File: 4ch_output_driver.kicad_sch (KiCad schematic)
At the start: 9 parts, among them U7 LTV-247

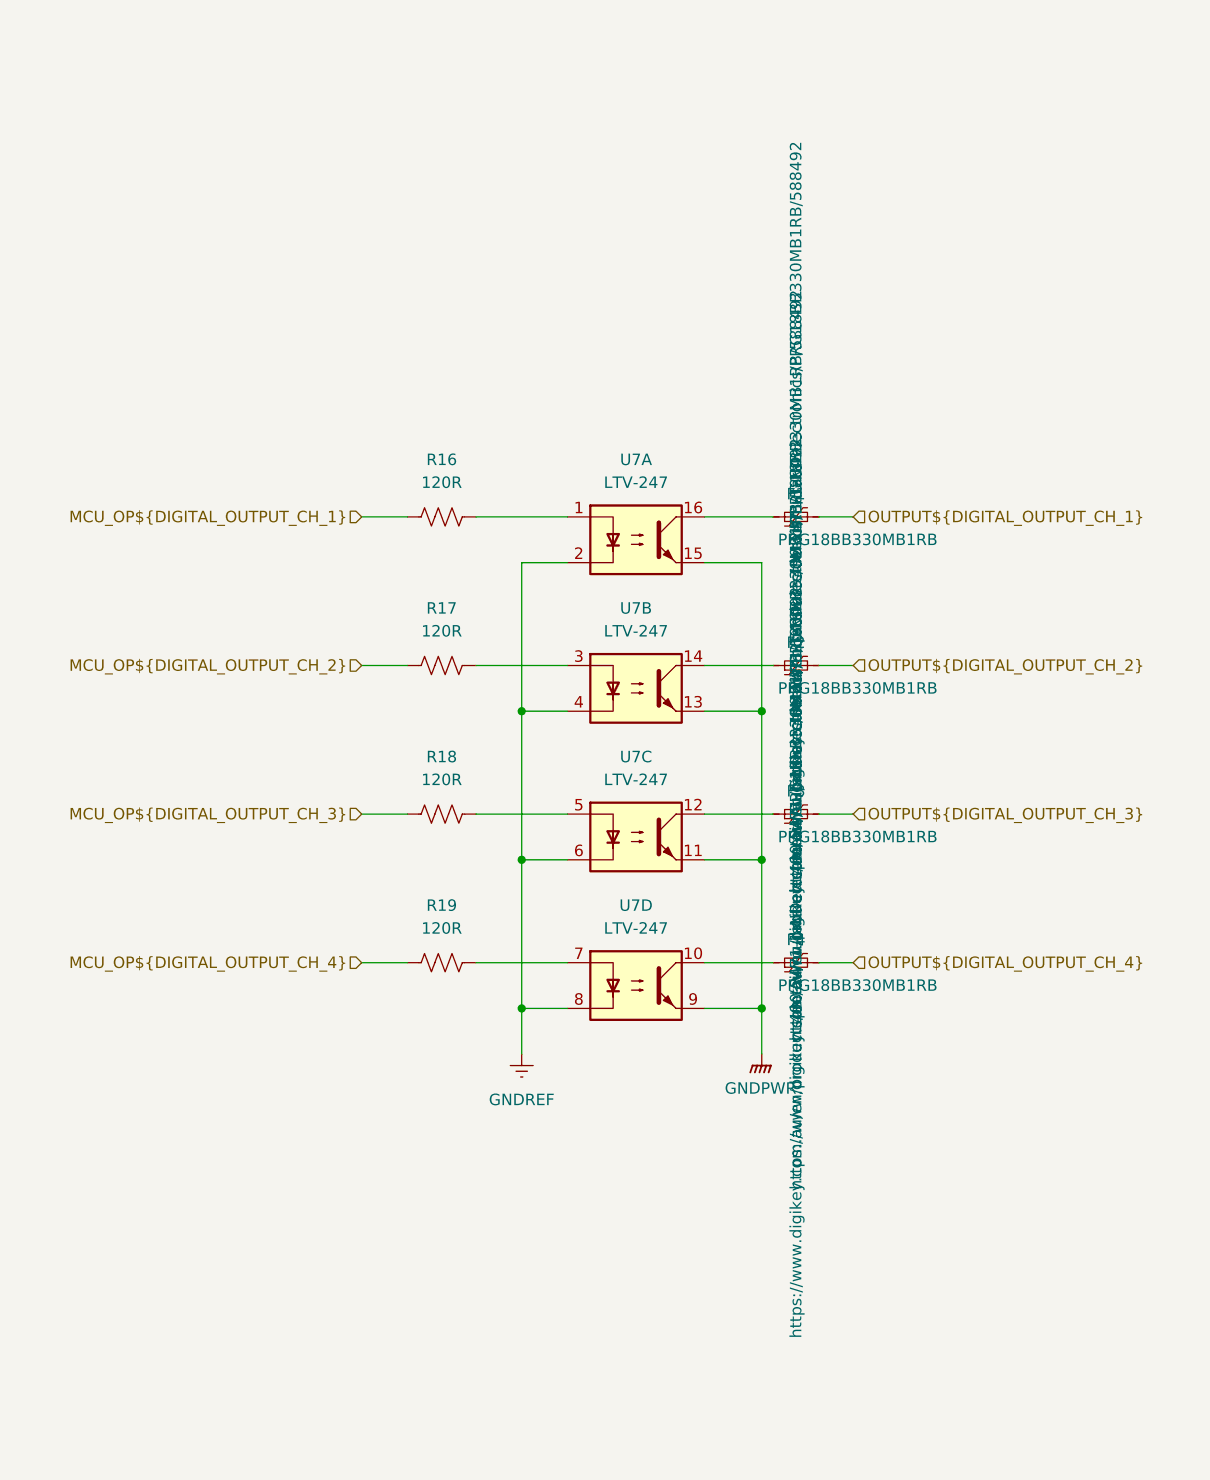
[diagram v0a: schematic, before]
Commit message: fix to annoying additional symbol fields displaying when we didn't want them to.
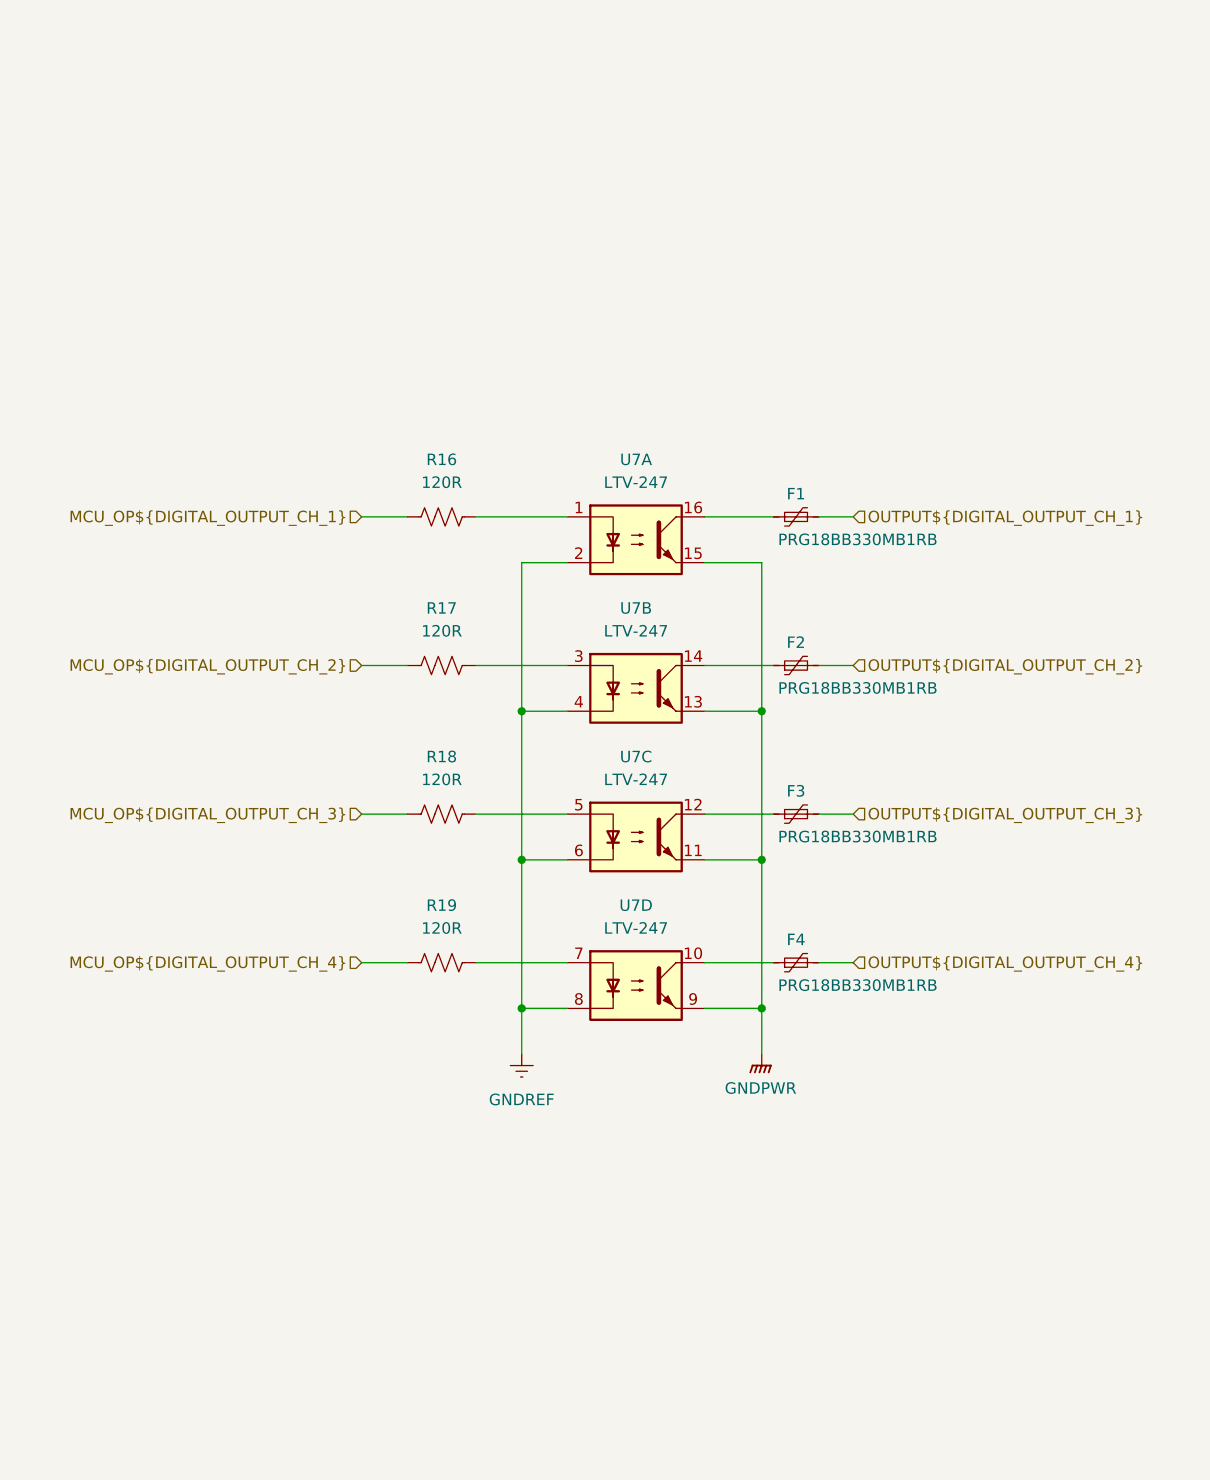
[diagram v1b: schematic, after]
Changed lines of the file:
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@@
 					(size 1.27 1.27)
 				)
+				(hide yes)
 			)
 		)
@@
 					(size 1.27 1.27)
 				)
+				(hide yes)
 			)
 		)
@@
 					(size 1.27 1.27)
 				)
+				(hide yes)
 			)
 		)
@@
 					(size 1.27 1.27)
 				)
+				(hide yes)
 			)
 		)
@@
 					(size 1.27 1.27)
 				)
+				(hide yes)
 			)
 		)
@@
 					(size 1.27 1.27)
 				)
+				(hide yes)
 			)
 		)
@@
 					(size 1.27 1.27)
 				)
+				(hide yes)
 			)
 		)
@@
 					(size 1.27 1.27)
 				)
+				(hide yes)
 			)
 		)
@@
 					(size 1.27 1.27)
 				)
+				(hide yes)
 			)
 		)
@@
 					(size 1.27 1.27)
 				)
+				(hide yes)
 			)
 		)
@@
 					(size 1.27 1.27)
 				)
+				(hide yes)
 			)
 		)
@@
 					(size 1.27 1.27)
 				)
+				(hide yes)
 			)
 		)
@@
 					(size 1.27 1.27)
 				)
+				(hide yes)
 			)
 		)
@@
 					(size 1.27 1.27)
 				)
+				(hide yes)
 			)
 		)
@@
 					(size 1.27 1.27)
 				)
+				(hide yes)
 			)
 		)
@@
 					(size 1.27 1.27)
 				)
+				(hide yes)
 			)
 		)
@@
 					(size 1.27 1.27)
 				)
+				(hide yes)
 			)
 		)
@@
 					(size 1.27 1.27)
 				)
+				(hide yes)
 			)
 		)
@@
 					(size 1.27 1.27)
 				)
+				(hide yes)
 			)
 		)
@@
 					(size 1.27 1.27)
 				)
+				(hide yes)
 			)
 		)
@@
 					(size 1.27 1.27)
 				)
+				(hide yes)
 			)
 		)
@@
 					(size 1.27 1.27)
 				)
+				(hide yes)
 			)
 		)
@@
 					(size 1.27 1.27)
 				)
+				(hide yes)
 			)
 		)
@@
 					(size 1.27 1.27)
 				)
-			)
-		)
+				(hide yes)
+			)
+		)

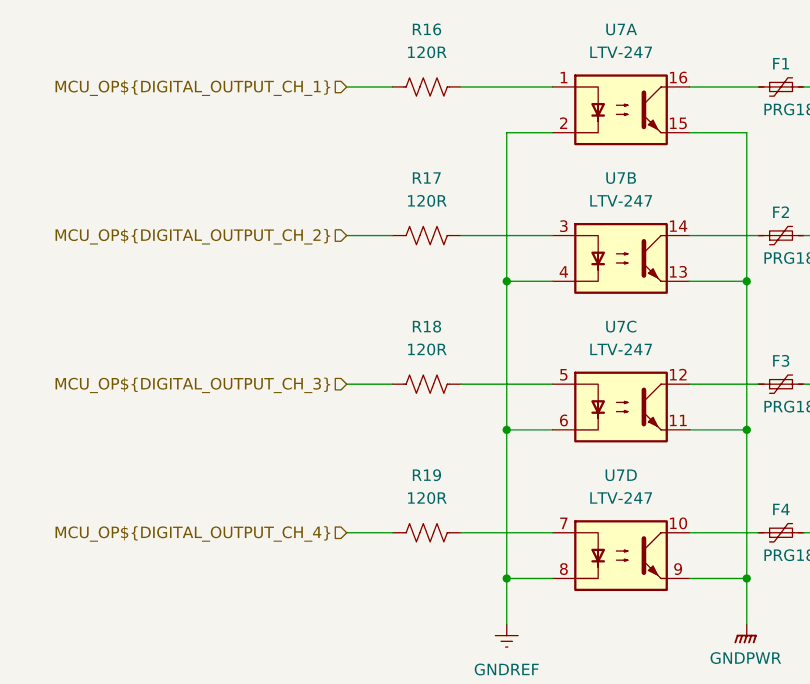
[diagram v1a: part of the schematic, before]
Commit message: BOM consolidation for various resistors. Moved BOM into symbol libraries and updated supplimentary BOM. Switched IO optical isolation circuitry to a more cost effective part.
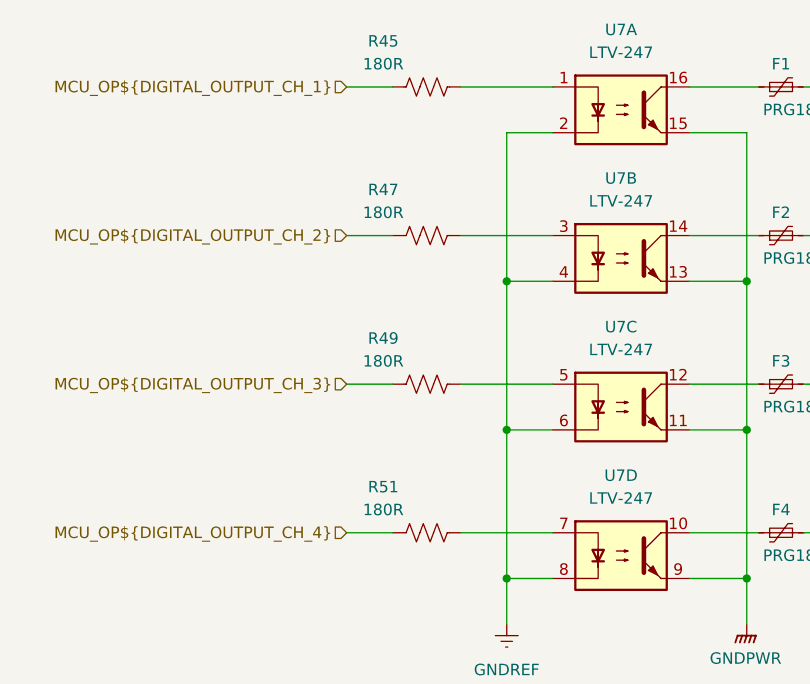
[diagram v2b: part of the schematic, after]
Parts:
- removed R16, R17, R18, R19: 120R, Resistor_SMD:R_1206_3216Metric_Pad1.30x1.75mm_HandSolder, symbol Device:R_US
- added R45, R47, R49, R51: 180R, Resistor_SMD:R_1206_3216Metric_Pad1.30x1.75mm_HandSolder, symbol Device:R_US
- U7: Digikey Part Number (none) -> 160-2255-1-ND; Digikey URL (none) -> https://www.digikey.com.au/en/products/detail/lite-on-inc/l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
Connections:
- net MCU_OP${DIGITAL_OUTPUT_CH_1}: now also R45.1
- net MCU_OP${DIGITAL_OUTPUT_CH_2}: now also R47.1
- net MCU_OP${DIGITAL_OUTPUT_CH_3}: now also R49.1
- net MCU_OP${DIGITAL_OUTPUT_CH_4}: now also R51.1
- net at U7.5: now also R49.2
- net at U7.7: now also R51.2
- net at U7.1: now also R45.2
- net at U7.3: now also R47.2

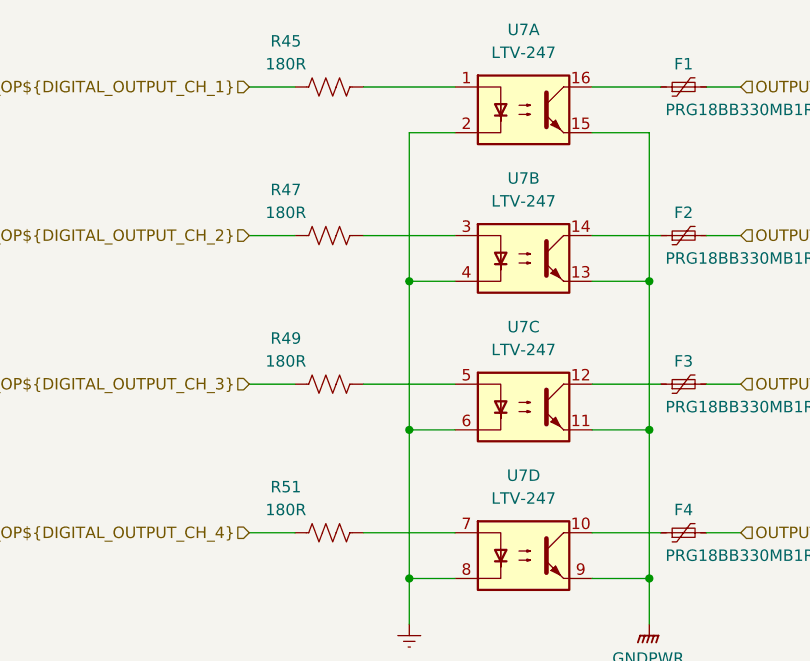
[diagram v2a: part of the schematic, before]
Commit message: New PSU designs + footprints assigned. Changes to board shape to make room for new components. BOM consolidation of supplimentary file
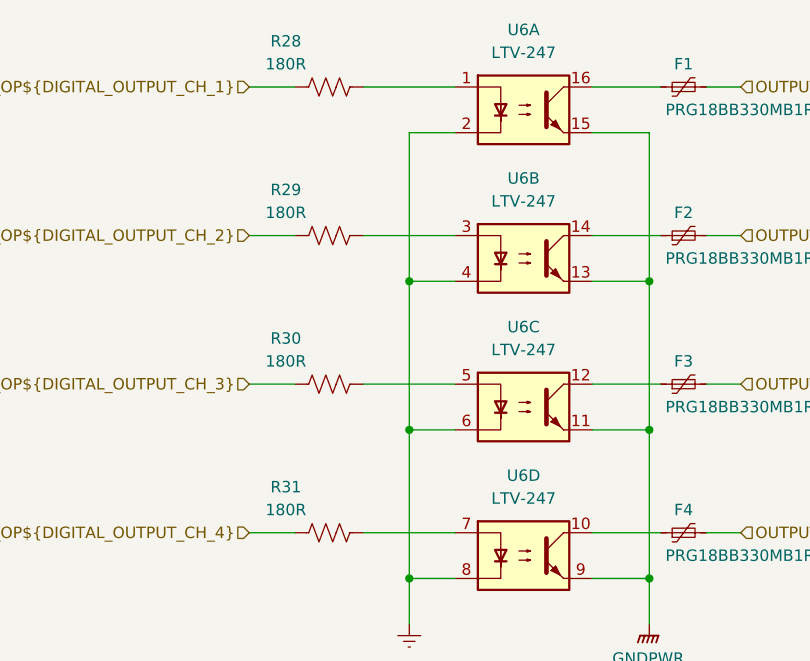
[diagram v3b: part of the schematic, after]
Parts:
- renumbered R45 to R28, R47 to R29, R49 to R30, R51 to R31, U7 to U6
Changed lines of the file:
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@@
 		(dnp no)
 		(fields_autoplaced yes)
-		(property "Reference" "U7"
+		(property "Reference" "U6"
 			(at 144.78 95.25 0)
 			(effects
@@
 				)
 				(path "/5473abc6-7b93-43cc-a401-f691c4d7d7cf/a10f9653-3098-46b3-8571-958500eea49a/75bfee9f-dba1-4332-b42b-f74c9030c21f"
-					(reference "U7")
+					(reference "U6")
 					(unit 3)
 				)
@@
 		(dnp no)
 		(fields_autoplaced yes)
-		(property "Reference" "U7"
+		(property "Reference" "U6"
 			(at 144.78 111.76 0)
 			(effects
@@
 				)
 				(path "/5473abc6-7b93-43cc-a401-f691c4d7d7cf/a10f9653-3098-46b3-8571-958500eea49a/75bfee9f-dba1-4332-b42b-f74c9030c21f"
-					(reference "U7")
+					(reference "U6")
 					(unit 4)
 				)
@@
 		(dnp no)
 		(fields_autoplaced yes)
-		(property "Reference" "U7"
+		(property "Reference" "U6"
 			(at 144.78 62.23 0)
 			(effects
@@
 				)
 				(path "/5473abc6-7b93-43cc-a401-f691c4d7d7cf/a10f9653-3098-46b3-8571-958500eea49a/75bfee9f-dba1-4332-b42b-f74c9030c21f"
-					(reference "U7")
+					(reference "U6")
 					(unit 1)
 				)
@@
 		(on_board yes)
 		(dnp no)
-		(property "Reference" "R49"
+		(property "Reference" "R30"
 			(at 118.364 96.52 90)
 			(effects
@@
 			(project "Remora Nucleo F446ZE Hat"
 				(path "/5473abc6-7b93-43cc-a401-f691c4d7d7cf/a10f9653-3098-46b3-8571-958500eea49a/389ca262-c58e-40b0-996c-af5bca34fee3"
-					(reference "R50")
-					(unit 1)
-				)
-				(path "/5473abc6-7b93-43cc-a401-f691c4d7d7cf/a10f9653-3098-46b3-8571-958500eea49a/75bfee9f-dba1-4332-b42b-f74c9030c21f"
-					(reference "R49")
+					(reference "R38")
+					(unit 1)
+				)
+				(path "/5473abc6-7b93-43cc-a401-f691c4d7d7cf/a10f9653-3098-46b3-8571-958500eea49a/75bfee9f-dba1-4332-b42b-f74c9030c21f"
+					(reference "R30")
 					(unit 1)
 				)
@@
 		(dnp no)
 		(fields_autoplaced yes)
-		(property "Reference" "U7"
+		(property "Reference" "U6"
 			(at 144.78 78.74 0)
 			(effects
@@
 				)
 				(path "/5473abc6-7b93-43cc-a401-f691c4d7d7cf/a10f9653-3098-46b3-8571-958500eea49a/75bfee9f-dba1-4332-b42b-f74c9030c21f"
-					(reference "U7")
+					(reference "U6")
 					(unit 2)
 				)
@@
 		(dnp no)
 		(fields_autoplaced yes)
-		(property "Reference" "#PWR077"
+		(property "Reference" "#PWR094"
 			(at 132.08 134.62 0)
 			(effects
@@
 			(project "Remora Nucleo F446ZE Hat"
 				(path "/5473abc6-7b93-43cc-a401-f691c4d7d7cf/a10f9653-3098-46b3-8571-958500eea49a/389ca262-c58e-40b0-996c-af5bca34fee3"
-					(reference "#PWR079")
-					(unit 1)
-				)
-				(path "/5473abc6-7b93-43cc-a401-f691c4d7d7cf/a10f9653-3098-46b3-8571-958500eea49a/75bfee9f-dba1-4332-b42b-f74c9030c21f"
-					(reference "#PWR077")
+					(reference "#PWR0104")
+					(unit 1)
+				)
+				(path "/5473abc6-7b93-43cc-a401-f691c4d7d7cf/a10f9653-3098-46b3-8571-958500eea49a/75bfee9f-dba1-4332-b42b-f74c9030c21f"
+					(reference "#PWR094")
 					(unit 1)
 				)
@@
 		(on_board yes)
 		(dnp no)
-		(property "Reference" "R45"
+		(property "Reference" "R28"
 			(at 118.364 63.5 90)
 			(effects
@@
 			(project "Remora Nucleo F446ZE Hat"
 				(path "/5473abc6-7b93-43cc-a401-f691c4d7d7cf/a10f9653-3098-46b3-8571-958500eea49a/389ca262-c58e-40b0-996c-af5bca34fee3"
-					(reference "R46")
-					(unit 1)
-				)
-				(path "/5473abc6-7b93-43cc-a401-f691c4d7d7cf/a10f9653-3098-46b3-8571-958500eea49a/75bfee9f-dba1-4332-b42b-f74c9030c21f"
-					(reference "R45")
+					(reference "R36")
+					(unit 1)
+				)
+				(path "/5473abc6-7b93-43cc-a401-f691c4d7d7cf/a10f9653-3098-46b3-8571-958500eea49a/75bfee9f-dba1-4332-b42b-f74c9030c21f"
+					(reference "R28")
 					(unit 1)
 				)
@@
 		(dnp no)
 		(fields_autoplaced yes)
-		(property "Reference" "#PWR078"
+		(property "Reference" "#PWR095"
 			(at 158.75 133.35 0)
 			(effects
@@
 			(project "Remora Nucleo F446ZE Hat"
 				(path "/5473abc6-7b93-43cc-a401-f691c4d7d7cf/a10f9653-3098-46b3-8571-958500eea49a/389ca262-c58e-40b0-996c-af5bca34fee3"
-					(reference "#PWR080")
-					(unit 1)
-				)
-				(path "/5473abc6-7b93-43cc-a401-f691c4d7d7cf/a10f9653-3098-46b3-8571-958500eea49a/75bfee9f-dba1-4332-b42b-f74c9030c21f"
-					(reference "#PWR078")
+					(reference "#PWR0105")
+					(unit 1)
+				)
+				(path "/5473abc6-7b93-43cc-a401-f691c4d7d7cf/a10f9653-3098-46b3-8571-958500eea49a/75bfee9f-dba1-4332-b42b-f74c9030c21f"
+					(reference "#PWR095")
 					(unit 1)
 				)
@@
 		(on_board yes)
 		(dnp no)
-		(property "Reference" "R47"
+		(property "Reference" "R29"
 			(at 118.364 80.01 90)
 			(effects
@@
 			(project "Remora Nucleo F446ZE Hat"
 				(path "/5473abc6-7b93-43cc-a401-f691c4d7d7cf/a10f9653-3098-46b3-8571-958500eea49a/389ca262-c58e-40b0-996c-af5bca34fee3"
-					(reference "R48")
-					(unit 1)
-				)
-				(path "/5473abc6-7b93-43cc-a401-f691c4d7d7cf/a10f9653-3098-46b3-8571-958500eea49a/75bfee9f-dba1-4332-b42b-f74c9030c21f"
-					(reference "R47")
+					(reference "R37")
+					(unit 1)
+				)
+				(path "/5473abc6-7b93-43cc-a401-f691c4d7d7cf/a10f9653-3098-46b3-8571-958500eea49a/75bfee9f-dba1-4332-b42b-f74c9030c21f"
+					(reference "R29")
 					(unit 1)
 				)
@@
 		(on_board yes)
 		(dnp no)
-		(property "Reference" "R51"
+		(property "Reference" "R31"
 			(at 118.364 113.03 90)
 			(effects
@@
 			(project "Remora Nucleo F446ZE Hat"
 				(path "/5473abc6-7b93-43cc-a401-f691c4d7d7cf/a10f9653-3098-46b3-8571-958500eea49a/389ca262-c58e-40b0-996c-af5bca34fee3"
-					(reference "R52")
-					(unit 1)
-				)
-				(path "/5473abc6-7b93-43cc-a401-f691c4d7d7cf/a10f9653-3098-46b3-8571-958500eea49a/75bfee9f-dba1-4332-b42b-f74c9030c21f"
-					(reference "R51")
-					(unit 1)
-				)
+					(reference "R39")
+					(unit 1)
+				)
+				(path "/5473abc6-7b93-43cc-a401-f691c4d7d7cf/a10f9653-3098-46b3-8571-958500eea49a/75bfee9f-dba1-4332-b42b-f74c9030c21f"
+					(reference "R31")
+					(unit 1)
+				)

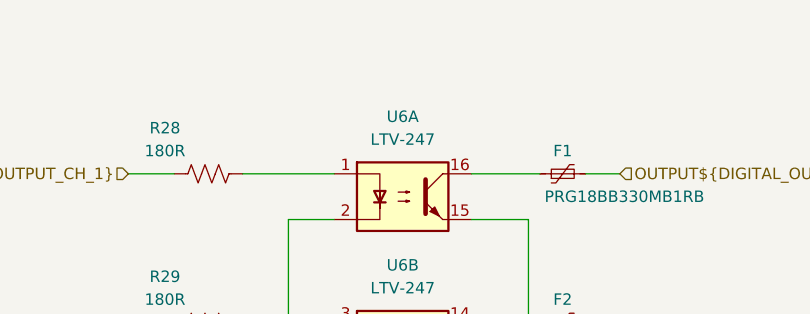
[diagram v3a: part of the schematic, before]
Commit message: Added high speed encoder input circuitry. General tidy and updates to readme
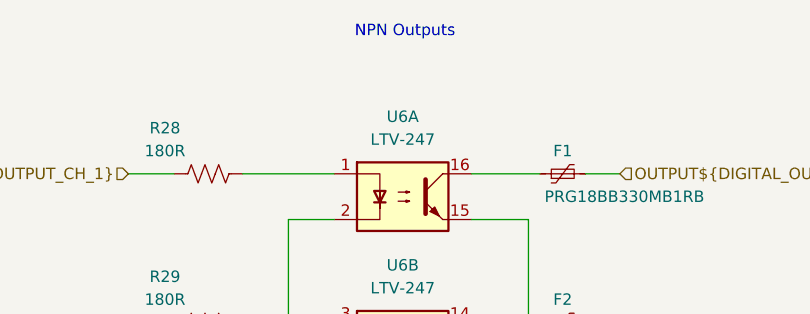
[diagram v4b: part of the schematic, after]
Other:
- note added: "NPN Outputs"
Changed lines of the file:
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@@
 	(generator_version "9.0")
 	(paper "A4")
+	(text "NPN Outputs"
+		(exclude_from_sim no)
+		(at 145.034 52.832 0)
+		(effects
+			(font
+				(size 1.27 1.27)
+			)
+		)
+	)
 	(junction
 		(at 158.75 106.68)
